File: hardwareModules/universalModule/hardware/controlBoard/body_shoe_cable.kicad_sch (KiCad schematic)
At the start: 2 parts, among them J42 SHOE, J43 B

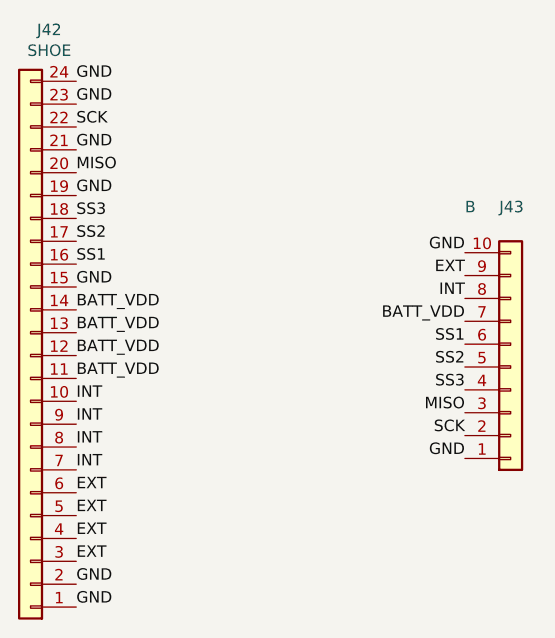
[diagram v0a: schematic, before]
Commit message: hardware: Add custom FPC cables
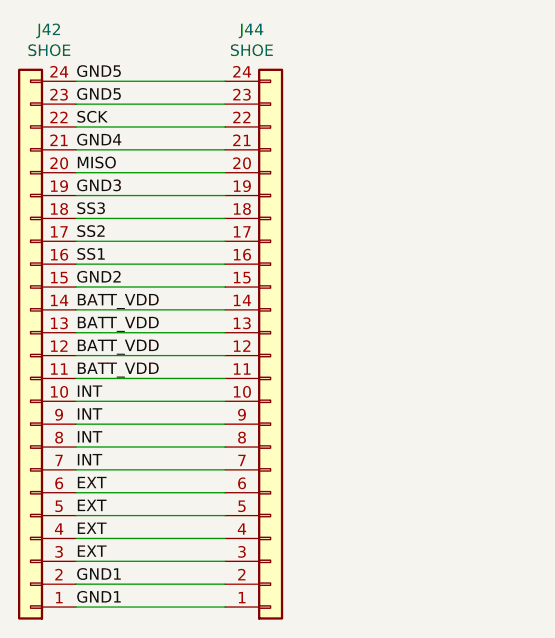
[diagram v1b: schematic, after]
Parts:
- removed J43: B, rofi:UM_SHOE_PADS_BOTH, symbol Connector_Generic:Conn_01x10
- added J44: SHOE, rofi:FPC_0.5_24_PADS, symbol Connector_Generic:Conn_01x24
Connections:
- net BATT_VDD: now also J44.11 (Pin_11), J44.12 (Pin_12), J44.13 (Pin_13), J44.14 (Pin_14)
- net EXT: now also J44.3 (Pin_3), J44.4 (Pin_4), J44.5 (Pin_5), J44.6 (Pin_6)
- net INT: now also J44.10 (Pin_10), J44.7 (Pin_7), J44.8 (Pin_8), J44.9 (Pin_9)
- net MISO: now also J44.20 (Pin_20)
- net SCK: now also J44.22 (Pin_22)
- net SS1: now also J44.16 (Pin_16)
- net SS2: now also J44.17 (Pin_17)
- net SS3: now also J44.18 (Pin_18)
- removed net GND: J42.1 (Pin_1), J42.15 (Pin_15), J42.19 (Pin_19), J42.2 (Pin_2), J42.21 (Pin_21), J42.23 (Pin_23), J42.24 (Pin_24)
- new net GND1: J42.1 (Pin_1), J42.2 (Pin_2), J44.1 (Pin_1), J44.2 (Pin_2)
- new net GND2: J42.15 (Pin_15), J44.15 (Pin_15)
- new net GND3: J42.19 (Pin_19), J44.19 (Pin_19)
- new net GND4: J42.21 (Pin_21), J44.21 (Pin_21)
- new net GND5: J42.23 (Pin_23), J42.24 (Pin_24), J44.23 (Pin_23), J44.24 (Pin_24)
